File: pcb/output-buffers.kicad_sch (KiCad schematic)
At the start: 0 parts

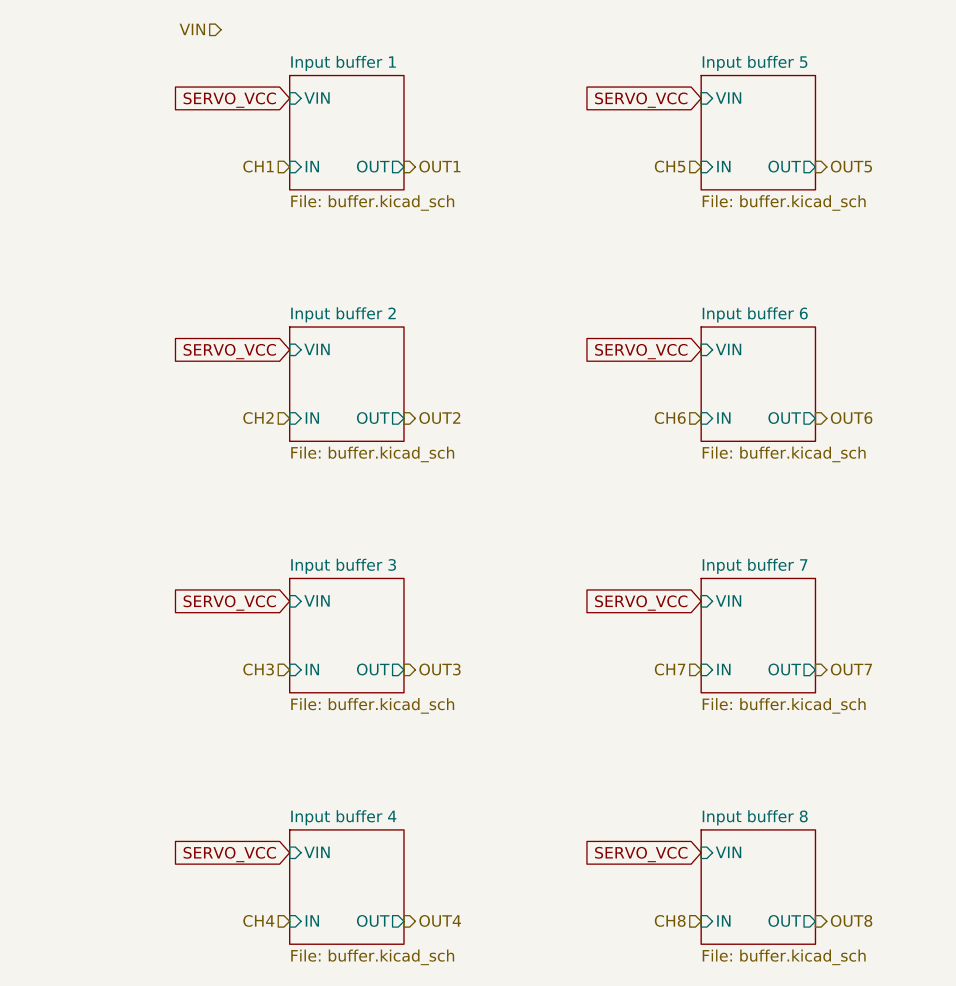
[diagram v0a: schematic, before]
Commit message: cleaned up buffer hierarchy
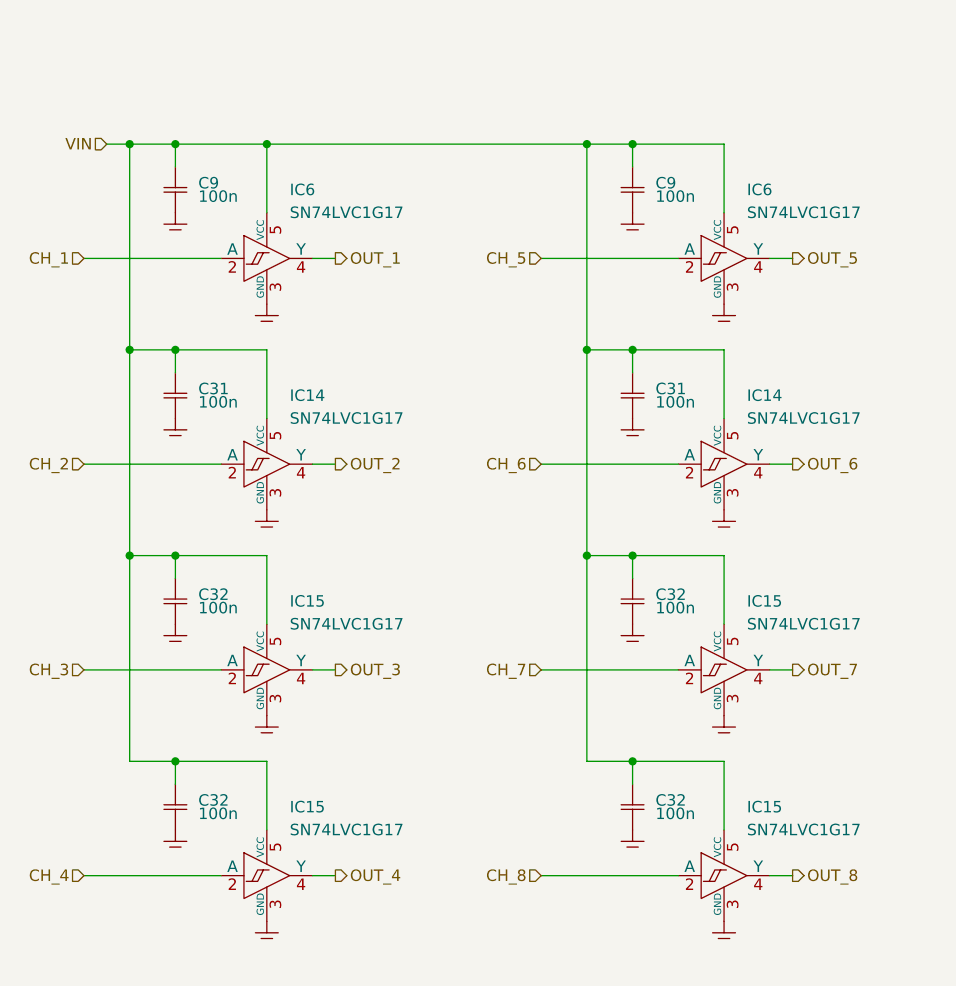
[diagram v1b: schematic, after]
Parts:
- added C31 (x2), C32 (x4), C9 (x2): 100n, SMT:0603, symbol generic:C
- added IC14 (x2), IC15 (x4), IC6 (x2): SN74LVC1G17, Single Schmitt-Trigger Buffer, symbol logic:SN74LVC1G17
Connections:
- net VIN: now also C31.2, C31.2, C32.2, C32.2, C32.2, C32.2, C9.2, C9.2, IC14.5 (VCC), IC14.5 (VCC), IC15.5 (VCC), IC15.5 (VCC), IC15.5 (VCC), IC15.5 (VCC), IC6.5 (VCC), IC6.5 (VCC)
- new net CH_1: IC6.2 (A)
- new net CH_2: IC14.2 (A)
- new net CH_3: IC15.2 (A)
- new net CH_4: IC15.2 (A)
- new net CH_5: IC6.2 (A)
- new net CH_6: IC14.2 (A)
- new net CH_7: IC15.2 (A)
- new net CH_8: IC15.2 (A)
- new net GND: C31.1, C31.1, C32.1, C32.1, C32.1, C32.1, C9.1, C9.1, IC14.3 (GND), IC14.3 (GND), IC15.3 (GND), IC15.3 (GND), IC15.3 (GND), IC15.3 (GND), IC6.3 (GND), IC6.3 (GND)
- new net OUT_1: IC6.4 (Y)
- new net OUT_2: IC14.4 (Y)
- new net OUT_3: IC15.4 (Y)
- new net OUT_4: IC15.4 (Y)
- new net OUT_5: IC6.4 (Y)
- new net OUT_6: IC14.4 (Y)
- new net OUT_7: IC15.4 (Y)
- new net OUT_8: IC15.4 (Y)
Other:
- removed sheet Input buffer 1
- removed sheet Input buffer 2
- removed sheet Input buffer 3
- removed sheet Input buffer 4
- removed sheet Input buffer 5
- removed sheet Input buffer 6
- removed sheet Input buffer 7
- removed sheet Input buffer 8

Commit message: added power switch for servos
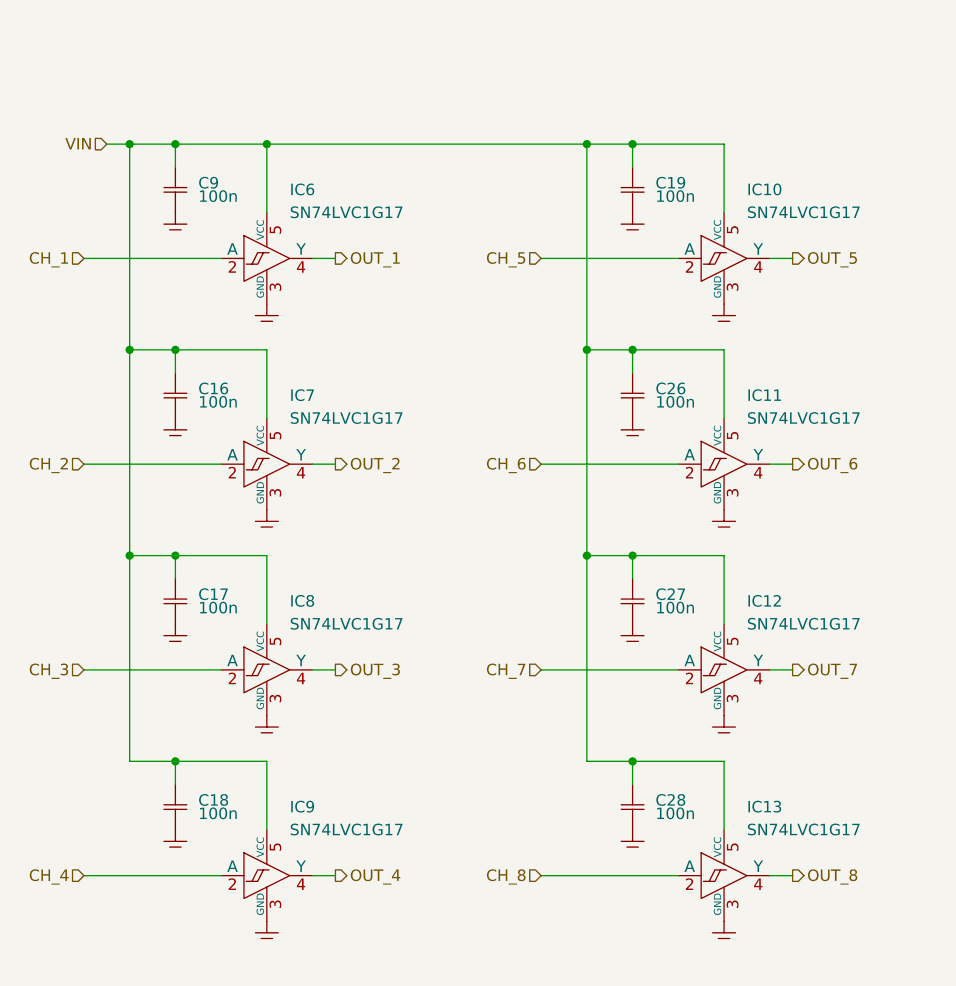
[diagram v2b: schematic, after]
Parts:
- IC10: renamed from IC6; footprint Single Schmitt-Trigger Buffer -> sc70:SC70-5L
- IC11, IC7: renamed from IC14; footprint Single Schmitt-Trigger Buffer -> sc70:SC70-5L
- IC12, IC13, IC8, IC9: renamed from IC15; footprint Single Schmitt-Trigger Buffer -> sc70:SC70-5L
- IC6: footprint Single Schmitt-Trigger Buffer -> sc70:SC70-5L
- renumbered C31 to C16, C32 to C17, C32 to C18, C9 to C19, C31 to C26, C32 to C27, C32 to C28

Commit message: worked on layout
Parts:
- renumbered C9 to C29, C16 to C30, C17 to C31, C18 to C32, C19 to C33, C26 to C34, C27 to C35, C28 to C36, IC6 to IC14, IC7 to IC15, IC8 to IC16, IC9 to IC17, IC10 to IC18, IC11 to IC19, IC12 to IC20, IC13 to IC21
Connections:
- net CH_1 renamed CH1
- net CH_2 renamed CH2
- net CH_3 renamed CH3
- net CH_4 renamed CH4
- net CH_5 renamed CH5
- net CH_6 renamed CH6
- net CH_7 renamed CH7
- net CH_8 renamed CH8
